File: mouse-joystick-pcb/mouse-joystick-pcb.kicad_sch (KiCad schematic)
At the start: 0 parts

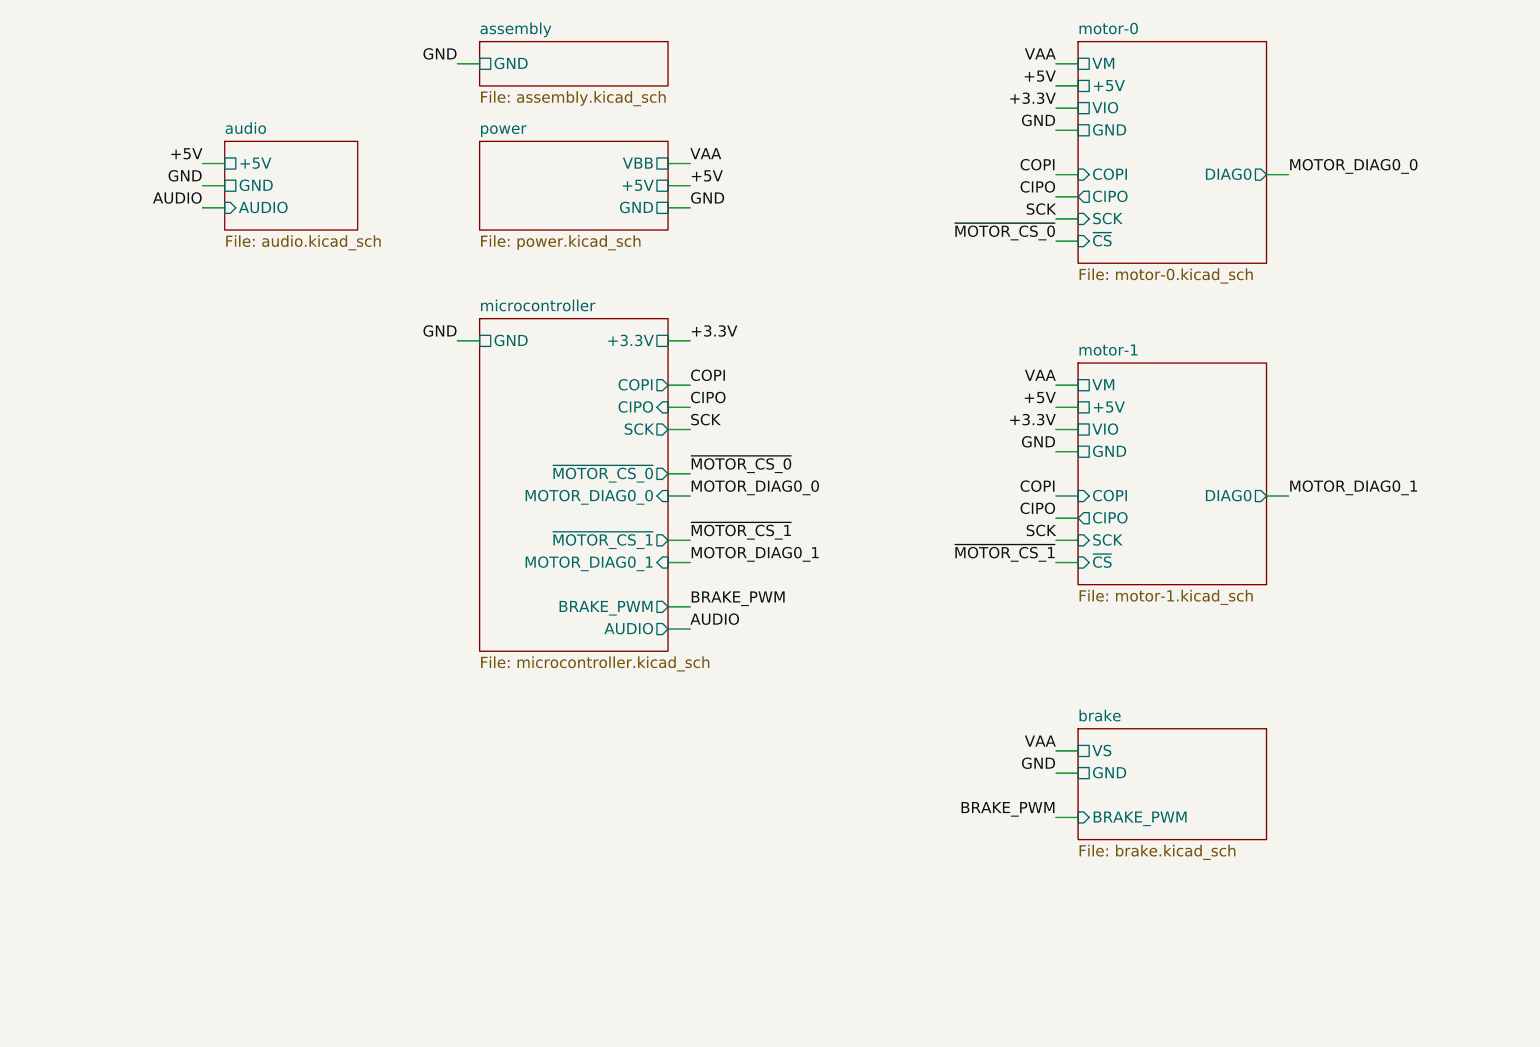
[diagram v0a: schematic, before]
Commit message: Add torque-sensor sheet
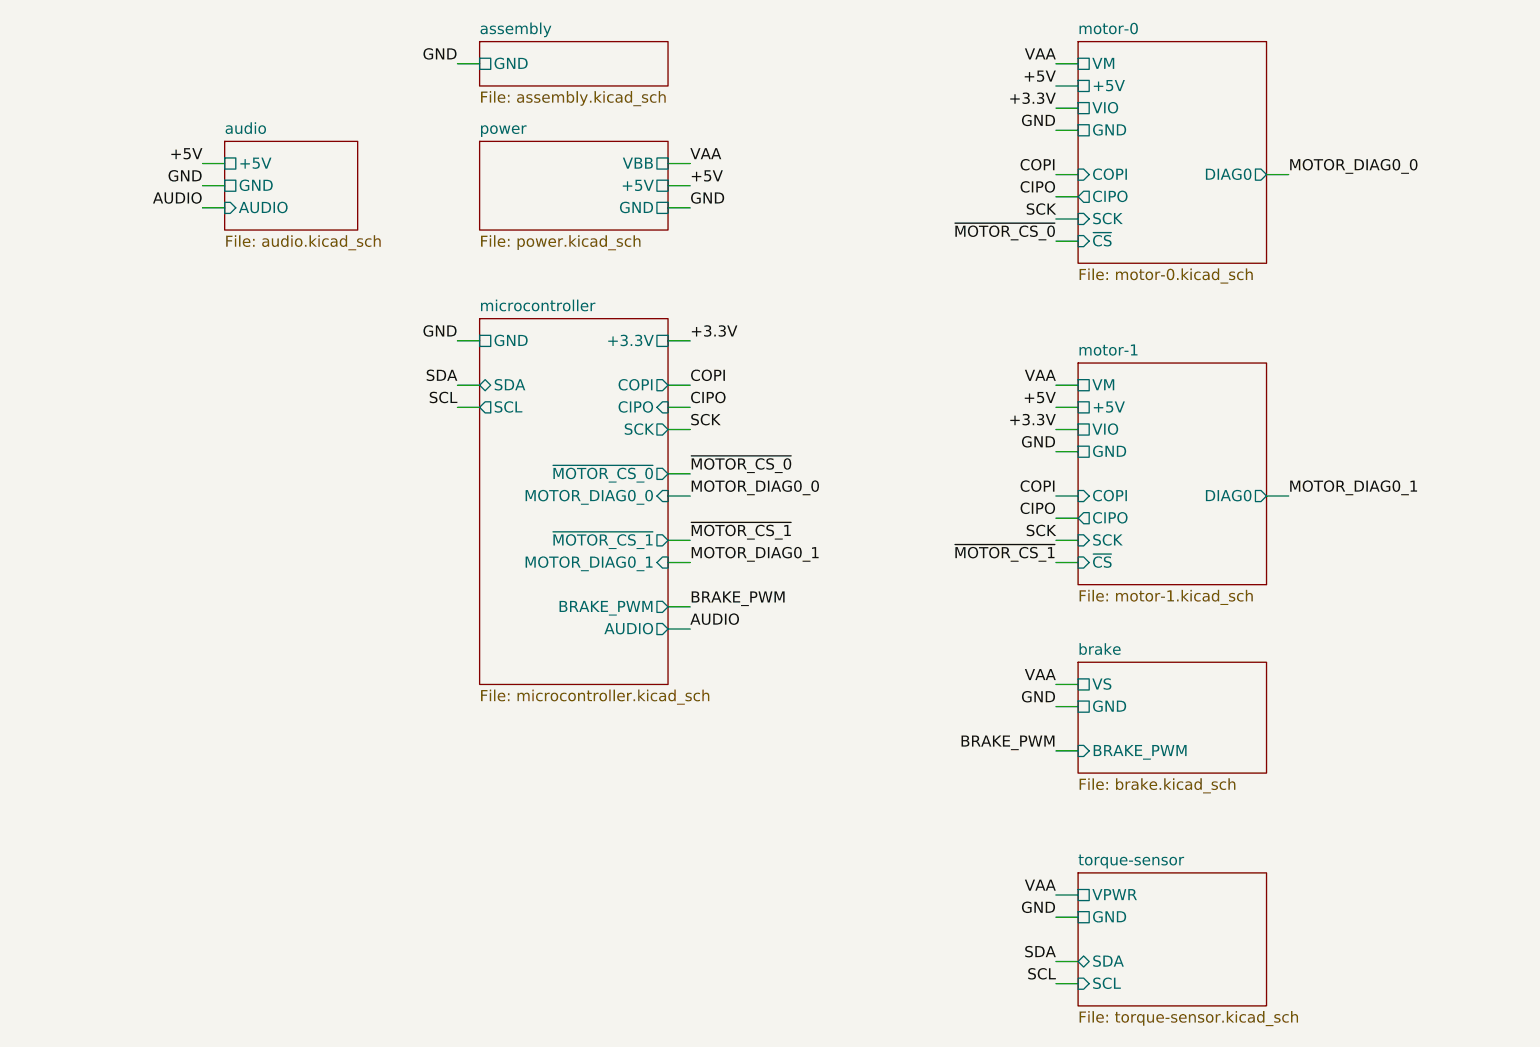
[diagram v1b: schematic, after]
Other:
- added sheet torque-sensor (torque-sensor.kicad_sch)
- sheet microcontroller ports: added SCL, SDA; removed none
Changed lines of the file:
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@@
   (title_block
     (title "mouse-joystick-pcb")
-    (date "2024-10-09")
+    (date "2024-10-11")
     (rev "1.0")
     (company "Peter Polidoro")
@@
     (stroke (width 0) (type default))
   )
+  (wire (pts (xy 69.85 93.98) (xy 72.39 93.98))
+    (stroke (width 0) (type default))
+  )
   (wire (pts (xy 138.43 54.61) (xy 140.97 54.61))
     (stroke (width 0) (type default))
@@
     (stroke (width 0) (type default))
   )
+  (wire (pts (xy 138.43 149.86) (xy 140.97 149.86))
+    (stroke (width 0) (type default))
+  )
   (wire (pts (xy 138.43 111.76) (xy 140.97 111.76))
     (stroke (width 0) (type default))
   )
-  (wire (pts (xy 138.43 140.97) (xy 140.97 140.97))
+  (wire (pts (xy 138.43 133.35) (xy 140.97 133.35))
     (stroke (width 0) (type default))
   )
@@
     (stroke (width 0) (type default))
   )
+  (wire (pts (xy 138.43 160.02) (xy 140.97 160.02))
+    (stroke (width 0) (type default))
+  )
   (wire (pts (xy 96.52 119.38) (xy 93.98 119.38))
     (stroke (width 0) (type default))
@@
     (stroke (width 0) (type default))
   )
+  (wire (pts (xy 138.43 157.48) (xy 140.97 157.48))
+    (stroke (width 0) (type default))
+  )
   (wire (pts (xy 96.52 109.22) (xy 93.98 109.22))
     (stroke (width 0) (type default))
@@
     (stroke (width 0) (type default))
   )
+  (wire (pts (xy 69.85 91.44) (xy 72.39 91.44))
+    (stroke (width 0) (type default))
+  )
   (wire (pts (xy 138.43 72.39) (xy 140.97 72.39))
     (stroke (width 0) (type default))
@@
     (stroke (width 0) (type default))
   )
-  (wire (pts (xy 138.43 133.35) (xy 140.97 133.35))
+  (wire (pts (xy 138.43 125.73) (xy 140.97 125.73))
     (stroke (width 0) (type default))
   )
@@
     (stroke (width 0) (type default))
   )
-  (wire (pts (xy 138.43 135.89) (xy 140.97 135.89))
+  (wire (pts (xy 138.43 128.27) (xy 140.97 128.27))
     (stroke (width 0) (type default))
   )
@@
     (stroke (width 0) (type default))
   )
+  (wire (pts (xy 138.43 152.4) (xy 140.97 152.4))
+    (stroke (width 0) (type default))
+  )
   (wire (pts (xy 138.43 57.15) (xy 140.97 57.15))
     (stroke (width 0) (type default))
@@
     (effects (font (size 1.27 1.27)) (justify right bottom))
   )
-  (label "VAA" (at 138.43 133.35 180) (fields_autoplaced)
+  (label "VAA" (at 138.43 125.73 180) (fields_autoplaced)
     (effects (font (size 1.27 1.27)) (justify right bottom))
   )
@@
     (effects (font (size 1.27 1.27)) (justify right bottom))
   )
+  (label "SDA" (at 69.85 91.44 180) (fields_autoplaced)
+    (effects (font (size 1.27 1.27)) (justify right bottom))
+  )
   (label "MOTOR_DIAG0_1" (at 165.1 104.14 0) (fields_autoplaced)
     (effects (font (size 1.27 1.27)) (justify left bottom))
@@
     (effects (font (size 1.27 1.27)) (justify right bottom))
   )
-  (label "BRAKE_PWM" (at 138.43 140.97 180) (fields_autoplaced)
+  (label "BRAKE_PWM" (at 138.43 133.35 180) (fields_autoplaced)
     (effects (font (size 1.27 1.27)) (justify right bottom))
   )
@@
     (effects (font (size 1.27 1.27)) (justify right bottom))
   )
+  (label "SDA" (at 138.43 157.48 180) (fields_autoplaced)
+    (effects (font (size 1.27 1.27)) (justify right bottom))
+  )
   (label "~{MOTOR_CS_0}" (at 96.52 101.6 0) (fields_autoplaced)
     (effects (font (size 1.27 1.27)) (justify left bottom))
   )
+  (label "SCL" (at 69.85 93.98 180) (fields_autoplaced)
+    (effects (font (size 1.27 1.27)) (justify right bottom))
+  )
   (label "COPI" (at 138.43 67.31 180) (fields_autoplaced)
     (effects (font (size 1.27 1.27)) (justify right bottom))
   )
-  (label "GND" (at 138.43 135.89 180) (fields_autoplaced)
+  (label "GND" (at 138.43 128.27 180) (fields_autoplaced)
     (effects (font (size 1.27 1.27)) (justify right bottom))
   )
@@
     (effects (font (size 1.27 1.27)) (justify left bottom))
   )
+  (label "GND" (at 138.43 152.4 180) (fields_autoplaced)
+    (effects (font (size 1.27 1.27)) (justify right bottom))
+  )
   (label "SCK" (at 138.43 109.22 180) (fields_autoplaced)
     (effects (font (size 1.27 1.27)) (justify right bottom))
@@
     (effects (font (size 1.27 1.27)) (justify right bottom))
   )
+  (label "VAA" (at 138.43 149.86 180) (fields_autoplaced)
+    (effects (font (size 1.27 1.27)) (justify right bottom))
+  )
+  (label "SCL" (at 138.43 160.02 180) (fields_autoplaced)
+    (effects (font (size 1.27 1.27)) (justify right bottom))
+  )
   (label "GND" (at 40.64 68.58 180) (fields_autoplaced)
     (effects (font (size 1.27 1.27)) (justify right bottom))
@@
     )
   )
+  (sheet (at 140.97 147.32) (size 21.59 15.24) (fields_autoplaced)
+    (stroke (width 0.1524) (type solid))
+    (fill (color 0 0 0 0.0000))
+    (property "Sheetname" "torque-sensor" (at 140.97 146.6084 0)
+      (effects (font (size 1.27 1.27)) (justify left bottom))
+    )
+    (property "Sheetfile" "torque-sensor.kicad_sch" (at 140.97 163.1446 0)
+      (effects (font (size 1.27 1.27)) (justify left top))
+    )
+    (pin "SCL" input (at 140.97 160.02 180)
+      (effects (font (size 1.27 1.27)) (justify left))
+    )
+    (pin "SDA" bidirectional (at 140.97 157.48 180)
+      (effects (font (size 1.27 1.27)) (justify left))
+    )
+    (pin "GND" passive (at 140.97 152.4 180)
+      (effects (font (size 1.27 1.27)) (justify left))
+    )
+    (pin "VPWR" passive (at 140.97 149.86 180)
+      (effects (font (size 1.27 1.27)) (justify left))
+    )
+    (instances
+      (project "mouse-joystick-pcb"
+        (path "/df2b2e89-e055-4140-95de-f1df723db034" (page "9"))
+      )
+    )
+  )
   (sheet (at 140.97 52.07) (size 21.59 25.4) (fields_autoplaced)
     (stroke (width 0.1524) (type solid))
@@
     )
   )
-  (sheet (at 72.39 83.82) (size 21.59 38.1) (fields_autoplaced)
+  (sheet (at 72.39 83.82) (size 21.59 41.91) (fields_autoplaced)
     (stroke (width 0.1524) (type solid))
     (fill (color 0 0 0 0.0000))
@@
       (effects (font (size 1.27 1.27)) (justify left bottom))
     )
-    (property "Sheetfile" "microcontroller.kicad_sch" (at 72.39 122.5046 0)
+    (property "Sheetfile" "microcontroller.kicad_sch" (at 72.39 126.3146 0)
       (effects (font (size 1.27 1.27)) (justify left top))
     )
@@
       (effects (font (size 1.27 1.27)) (justify right))
     )
+    (pin "SDA" bidirectional (at 72.39 91.44 180)
+      (effects (font (size 1.27 1.27)) (justify left))
+    )
+    (pin "SCL" output (at 72.39 93.98 180)
+      (effects (font (size 1.27 1.27)) (justify left))
+    )
     (instances
       (project "mouse-joystick-pcb"
@@
     )
   )
-  (sheet (at 140.97 130.81) (size 21.59 12.7) (fields_autoplaced)
-    (stroke (width 0.1524) (type solid))
-    (fill (color 0 0 0 0.0000))
-    (property "Sheetname" "brake" (at 140.97 130.0984 0)
-      (effects (font (size 1.27 1.27)) (justify left bottom))
-    )
-    (property "Sheetfile" "brake.kicad_sch" (at 140.97 144.0946 0)
-      (effects (font (size 1.27 1.27)) (justify left top))
-    )
-    (pin "VS" passive (at 140.97 133.35 180)
-      (effects (font (size 1.27 1.27)) (justify left))
-    )
-    (pin "GND" passive (at 140.97 135.89 180)
-      (effects (font (size 1.27 1.27)) (justify left))
-    )
-    (pin "BRAKE_PWM" input (at 140.97 140.97 180)
-      (effects (font (size 1.27 1.27)) (justify left))
-    )
+  (sheet (at 140.97 123.19) (size 21.59 12.7) (fields_autoplaced)
+    (stroke (width 0.1524) (type solid))
+    (fill (color 0 0 0 0.0000))
+    (property "Sheetname" "brake" (at 140.97 122.4784 0)
+      (effects (font (size 1.27 1.27)) (justify left bottom))
+    )
+    (property "Sheetfile" "brake.kicad_sch" (at 140.97 136.4746 0)
+      (effects (font (size 1.27 1.27)) (justify left top))
+    )
+    (pin "VS" passive (at 140.97 125.73 180)
+      (effects (font (size 1.27 1.27)) (justify left))
+    )
+    (pin "GND" passive (at 140.97 128.27 180)
+      (effects (font (size 1.27 1.27)) (justify left))
+    )
+    (pin "BRAKE_PWM" input (at 140.97 133.35 180)
+      (effects (font (size 1.27 1.27)) (justify left))
+    )

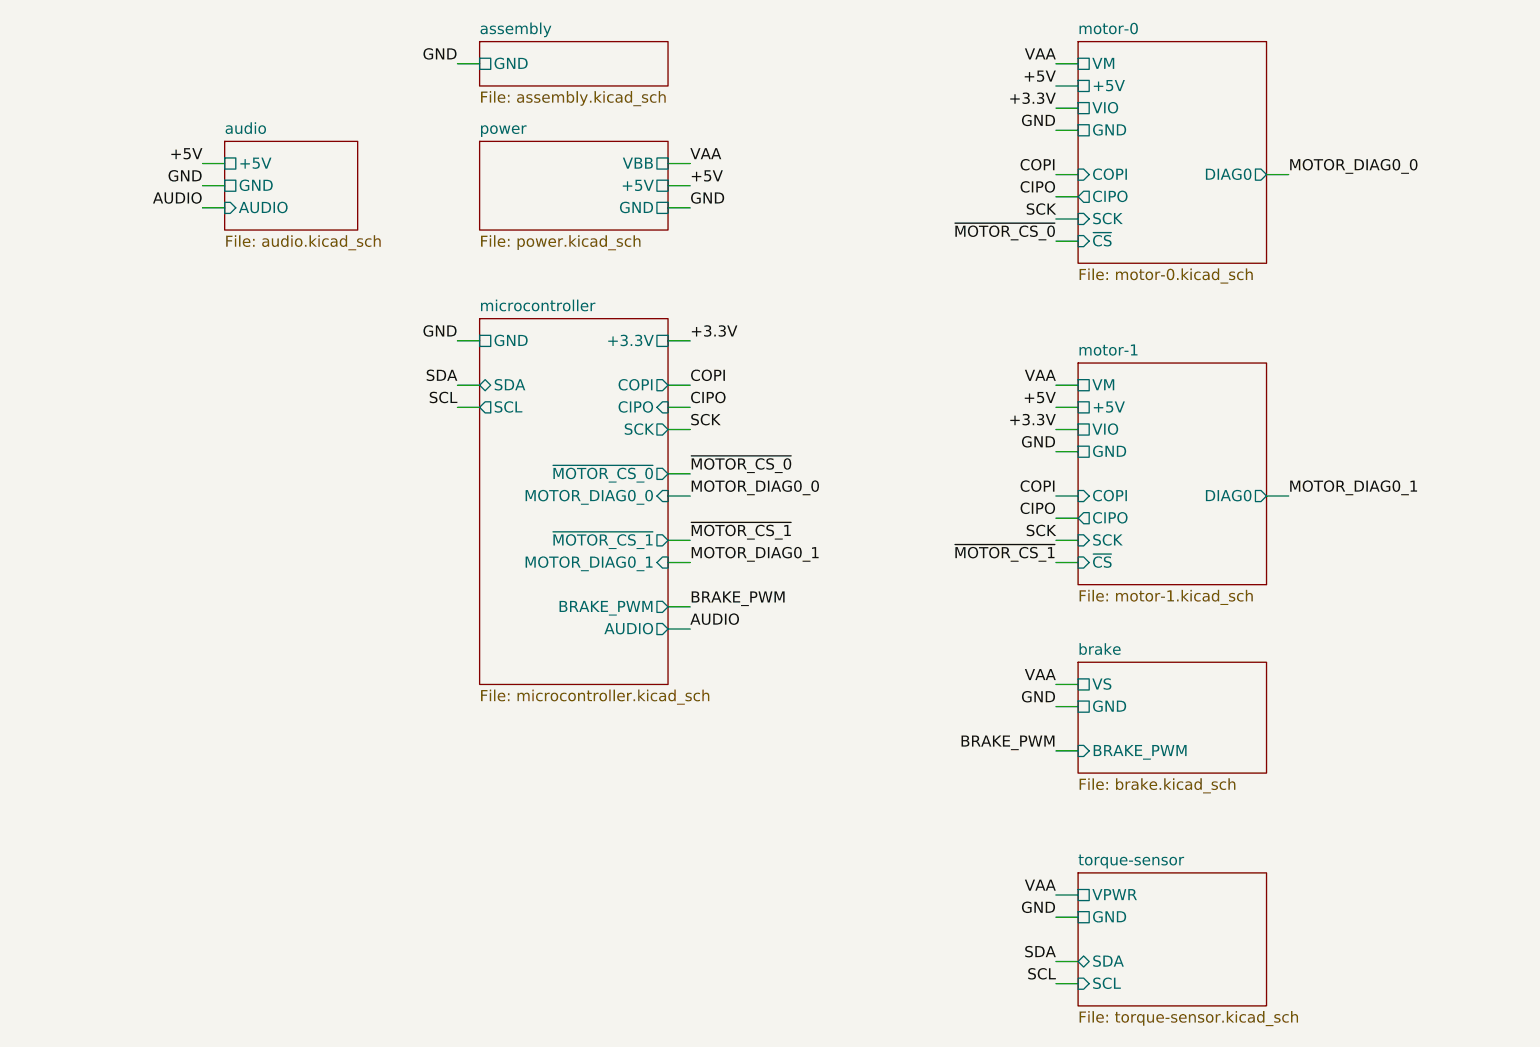
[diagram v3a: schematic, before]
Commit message: Rename schematic sheets
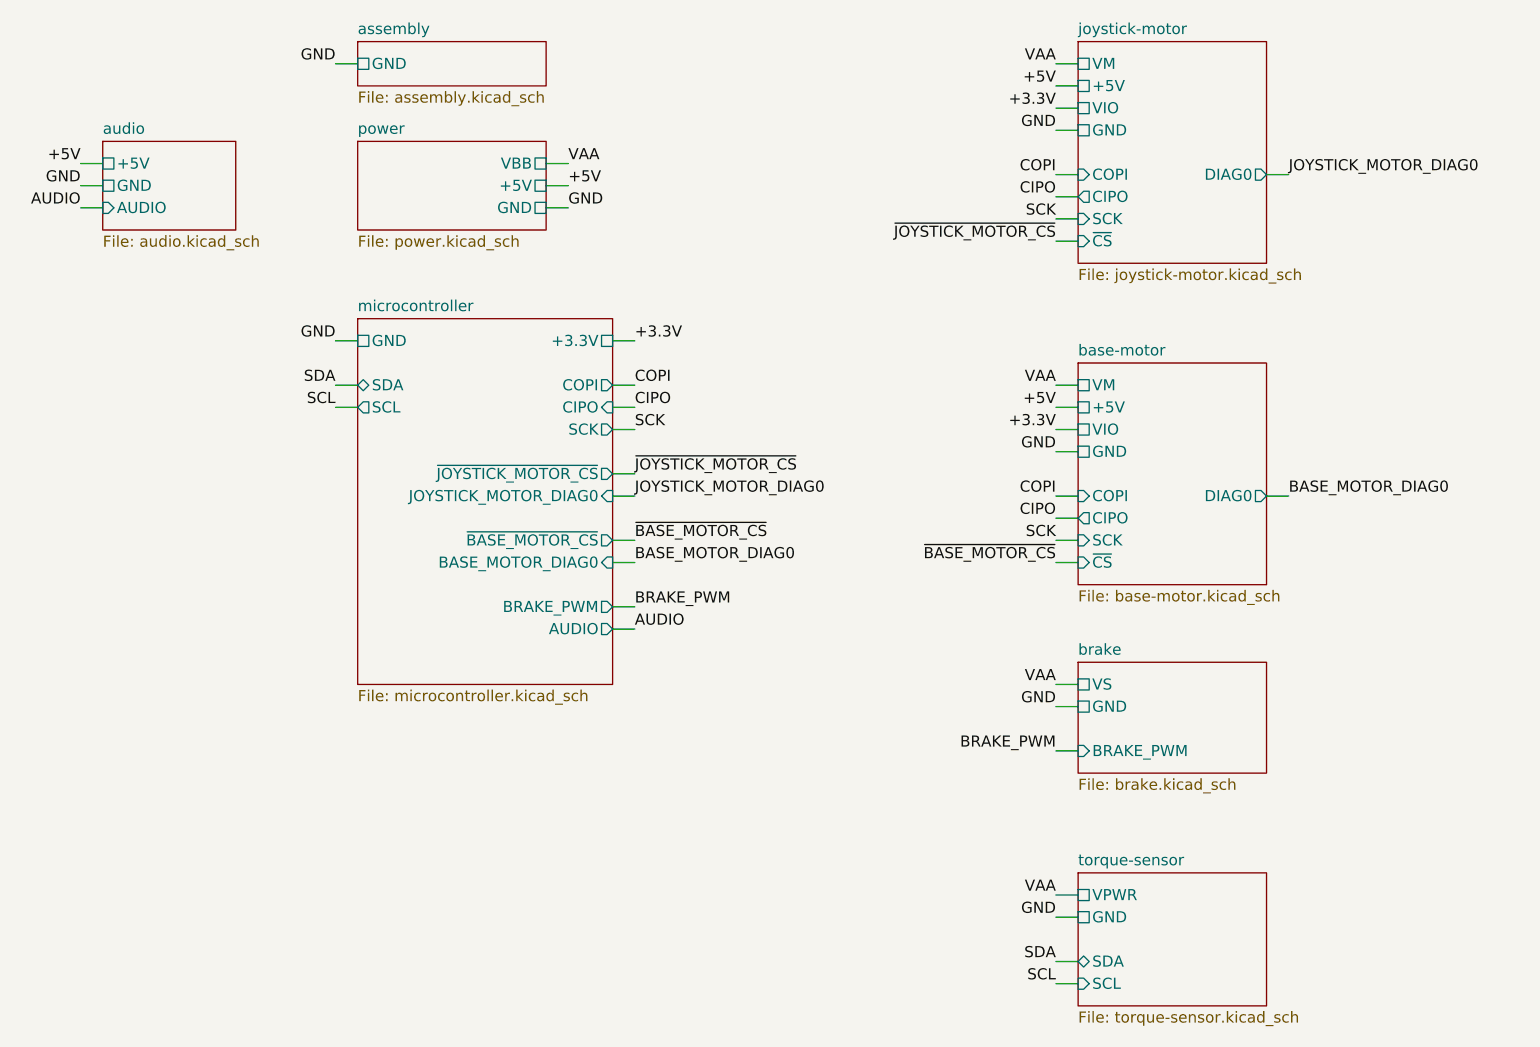
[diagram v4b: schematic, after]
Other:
- sheet motor-0 renamed joystick-motor
- sheet motor-1 renamed base-motor
- sheet base-motor: file motor-1.kicad_sch -> base-motor.kicad_sch
- sheet joystick-motor: file motor-0.kicad_sch -> joystick-motor.kicad_sch
- sheet microcontroller ports: added BASE_MOTOR_DIAG0, JOYSTICK_MOTOR_DIAG0, ~{BASE_MOTOR_CS}, ~{JOYSTICK_MOTOR_CS}; removed MOTOR_DIAG0_0, MOTOR_DIAG0_1, ~{MOTOR_CS_0}, ~{MOTOR_CS_1}
